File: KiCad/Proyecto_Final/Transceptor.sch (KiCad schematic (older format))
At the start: 51 parts, among them T1 2450BL05A0100, U1 MAX1193ETI+, U2 MAX2837

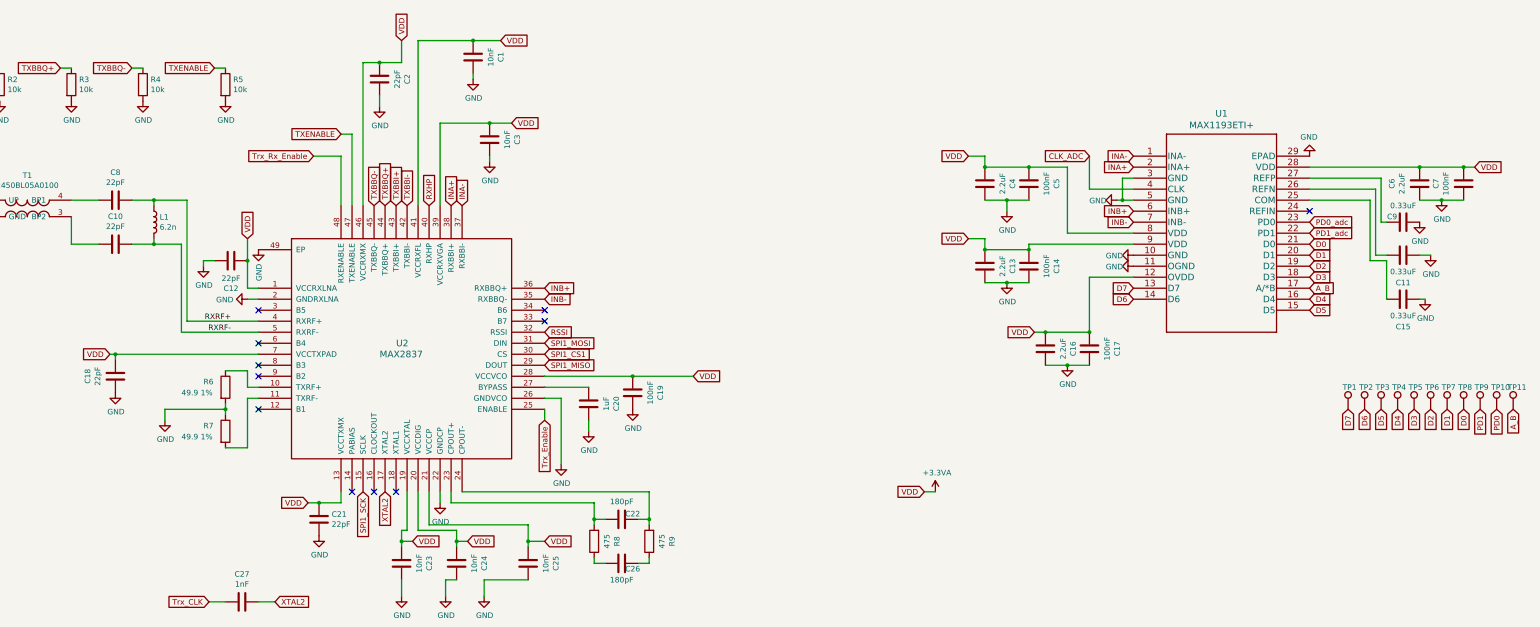
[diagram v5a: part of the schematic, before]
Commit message: Pistas reacomodadas para mejor ruteo.
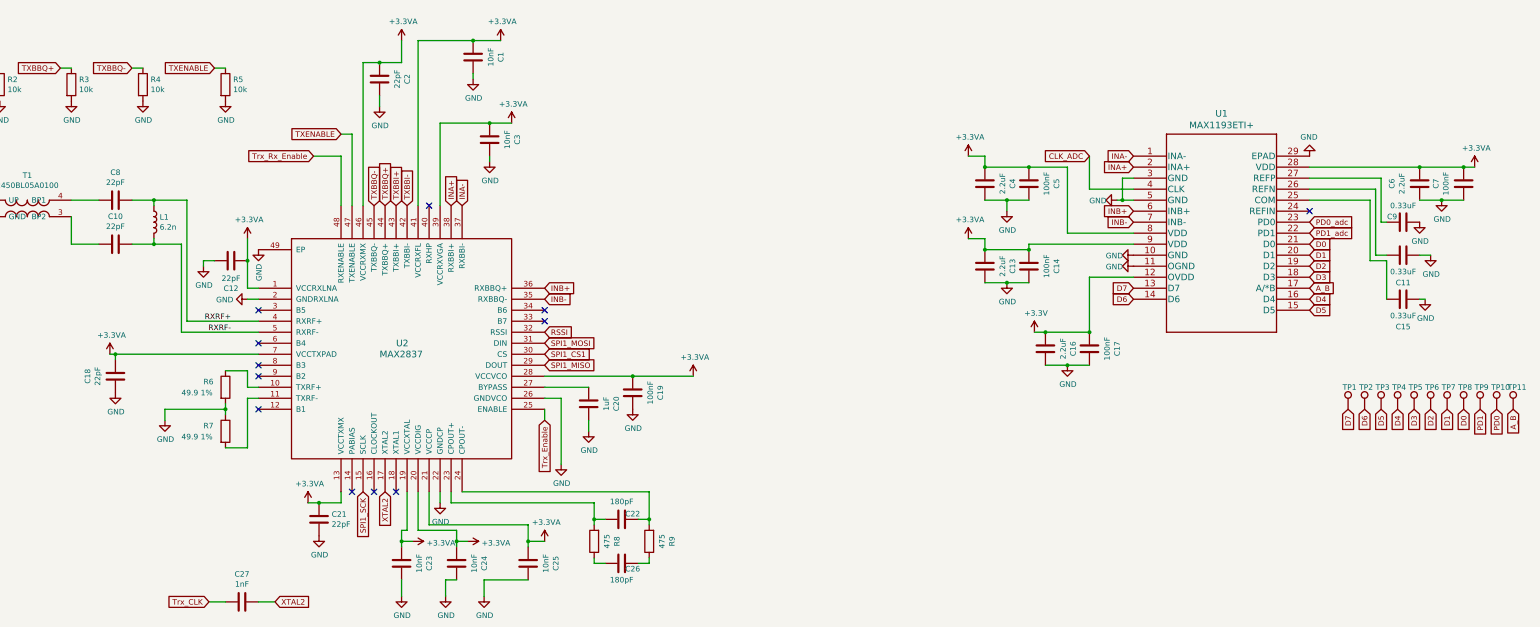
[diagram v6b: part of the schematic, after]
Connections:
- net +3.3VA: no longer C16.2, C17.2, U1.12 (OVDD)
- net RXHP: no longer names the net of U2.40 (RXHP)
- new net +3V3: C16.2, C17.2, U1.12 (OVDD)
- no-connect marks 11 -> 12
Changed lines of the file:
@@
 Wire Wire Line
 	5650 5950 5650 5800
-Text GLabel 5750 5450 2    50   Input ~ 0
-VDD
 Connection ~ 5650 5450
 Wire Wire Line
@@
 	1    0    0    -1
 $EndComp
-Text GLabel 6250 5450 2    50   Input ~ 0
-VDD
 Wire Wire Line
 	6050 5800 6050 5950
@@
 	-1   0    0    1
 $EndComp
-Text GLabel 6950 5450 2    50   Input ~ 0
-VDD
 Wire Wire Line
 	5900 5300 6800 5300
@@
 	1    0    0    -1
 $EndComp
-Text GLabel 8300 3950 2    50   Input ~ 0
-VDD
 Text GLabel 6950 3850 2    50   Input ~ 0
 SPI1_MISO
@@
 Wire Wire Line
 	6000 2400 6000 1650
-Text GLabel 6650 1650 2    50   Input ~ 0
-VDD
 Wire Wire Line
 	6650 1650 6450 1650
 Connection ~ 6450 1650
-Text GLabel 6550 900  2    50   Input ~ 0
-VDD
 $Comp
 L Device:C C1
@@
 Wire Wire Line
 	5450 1500 5450 1400
-Text GLabel 5650 900  1    50   Input ~ 0
-VDD
 Wire Wire Line
 	5650 900  5650 1100
@@
 Wire Wire Line
 	10800 1950 10950 1950
-Text GLabel 10800 1950 0    50   Input ~ 0
-VDD
 Wire Wire Line
 	11150 2350 10950 2350
@@
 Wire Wire Line
 	10950 2800 11350 2800
-Text GLabel 10800 2700 0    50   Input ~ 0
-VDD
 Wire Wire Line
 	10800 2700 10950 2700
@@
 	-1   0    0    1
 $EndComp
-Text GLabel 11400 3550 0    50   Input ~ 0
-VDD
 Wire Wire Line
 	11900 3050 12300 3050
-Text GLabel 15400 2050 2    50   Input ~ 0
-VDD
 Connection ~ 11900 3550
 $Comp
@@
 	1    0    0    -1
 $EndComp
-Text GLabel 3000 3750 0    50   Input ~ 0
-VDD
-Text GLabel 4250 2700 1    50   Input ~ 0
-VDD
 Wire Wire Line
 	4250 2700 4250 2900
@@
 Wire Wire Line
 	5100 5100 4900 5100
-Text GLabel 4800 5100 0    50   Input ~ 0
-VDD
 Wire Wire Line
 	4800 5100 4900 5100
@@
 Text GLabel 1300 1150 0    50   Input ~ 0
 TXBBI-
-Text GLabel 5900 2400 1    50   Input ~ 0
-RXHP
 Wire Wire Line
 	6000 1650 6450 1650
@@
 	11900 2250 12300 2250
 NoConn ~ 13900 2450
-Text GLabel 10400 5000 0    50   Input ~ 0
-VDD
-Wire Wire Line
-	10400 5000 10500 5000
 NoConn ~ 5600 5000
 $Comp
@@
 Wire Wire Line
 	4050 4250 4050 4300
-$Comp
-L power:+3.3VA #PWR?
-U 1 1 60A0F8F4
-P 10500 5000
-F 0 "#PWR?" H 10500 4850 50  0001 C CNN
-F 1 "+3.3VA" H 10515 5173 50  0000 C CNN
-F 2 "" H 10500 5000 50  0001 C CNN
-F 3 "" H 10500 5000 50  0001 C CNN
-	1    10500 5000
-	1    0    0    -1
-$EndComp
+NoConn ~ 5900 2400
+$Comp
+L power:+3.3VA #PWR0132
+U 1 1 609C56C0
+P 8300 3950
+F 0 "#PWR0132" H 8300 3800 50  0001 C CNN
+F 1 "+3.3VA" H 8315 4123 50  0000 C CNN
+F 2 "" H 8300 3950 50  0001 C CNN
+F 3 "" H 8300 3950 50  0001 C CNN
+	1    8300 3950
+	1    0    0    -1
+$EndComp
+$Comp
+L power:+3.3VA #PWR0133
+U 1 1 609C63F1
+P 6950 5450
+F 0 "#PWR0133" H 6950 5300 50  0001 C CNN
+F 1 "+3.3VA" H 6965 5623 50  0000 C CNN
+F 2 "" H 6950 5450 50  0001 C CNN
+F 3 "" H 6950 5450 50  0001 C CNN
+	1    6950 5450
+	1    0    0    -1
+$EndComp
+$Comp
+L power:+3.3VA #PWR0134
+U 1 1 609C66C1
+P 6250 5450
+F 0 "#PWR0134" H 6250 5300 50  0001 C CNN
+F 1 "+3.3VA" V 6265 5578 50  0000 L CNN
+F 2 "" H 6250 5450 50  0001 C CNN
+F 3 "" H 6250 5450 50  0001 C CNN
+	1    6250 5450
+	0    1    1    0
+$EndComp
+$Comp
+L power:+3.3VA #PWR0135
+U 1 1 609C6F0F
+P 5750 5450
+F 0 "#PWR0135" H 5750 5300 50  0001 C CNN
+F 1 "+3.3VA" V 5765 5578 50  0000 L CNN
+F 2 "" H 5750 5450 50  0001 C CNN
+F 3 "" H 5750 5450 50  0001 C CNN
+	1    5750 5450
+	0    1    1    0
+$EndComp
+$Comp
+L power:+3.3VA #PWR0136
+U 1 1 609C777F
+P 4800 5100
+F 0 "#PWR0136" H 4800 4950 50  0001 C CNN
+F 1 "+3.3VA" H 4815 5273 50  0000 C CNN
+F 2 "" H 4800 5100 50  0001 C CNN
+F 3 "" H 4800 5100 50  0001 C CNN
+	1    4800 5100
+	1    0    0    -1
+$EndComp
+$Comp
+L power:+3.3VA #PWR0137
+U 1 1 609C8000
+P 3000 3750
+F 0 "#PWR0137" H 3000 3600 50  0001 C CNN
+F 1 "+3.3VA" H 3015 3923 50  0000 C CNN
+F 2 "" H 3000 3750 50  0001 C CNN
+F 3 "" H 3000 3750 50  0001 C CNN
+	1    3000 3750
+	1    0    0    -1
+$EndComp
+$Comp
+L power:+3.3VA #PWR0138
+U 1 1 609C88CB
+P 4250 2700
+F 0 "#PWR0138" H 4250 2550 50  0001 C CNN
+F 1 "+3.3VA" H 4265 2873 50  0000 C CNN
+F 2 "" H 4250 2700 50  0001 C CNN
+F 3 "" H 4250 2700 50  0001 C CNN
+	1    4250 2700
+	1    0    0    -1
+$EndComp
+$Comp
+L power:+3.3VA #PWR0139
+U 1 1 609C914C
+P 5650 900
+F 0 "#PWR0139" H 5650 750 50  0001 C CNN
+F 1 "+3.3VA" H 5665 1073 50  0000 C CNN
+F 2 "" H 5650 900 50  0001 C CNN
+F 3 "" H 5650 900 50  0001 C CNN
+	1    5650 900
+	1    0    0    -1
+$EndComp
+$Comp
+L power:+3.3VA #PWR0140
+U 1 1 609C9988
+P 6550 900
+F 0 "#PWR0140" H 6550 750 50  0001 C CNN
+F 1 "+3.3VA" H 6565 1073 50  0000 C CNN
+F 2 "" H 6550 900 50  0001 C CNN
+F 3 "" H 6550 900 50  0001 C CNN
+	1    6550 900
+	1    0    0    -1
+$EndComp
+$Comp
+L power:+3.3VA #PWR0141
+U 1 1 609CA2CB
+P 6650 1650
+F 0 "#PWR0141" H 6650 1500 50  0001 C CNN
+F 1 "+3.3VA" H 6665 1823 50  0000 C CNN
+F 2 "" H 6650 1650 50  0001 C CNN
+F 3 "" H 6650 1650 50  0001 C CNN
+	1    6650 1650
+	1    0    0    -1
+$EndComp
+$Comp
+L power:+3.3VA #PWR0142
+U 1 1 609CB87B
+P 10800 1950
+F 0 "#PWR0142" H 10800 1800 50  0001 C CNN
+F 1 "+3.3VA" H 10815 2123 50  0000 C CNN
+F 2 "" H 10800 1950 50  0001 C CNN
+F 3 "" H 10800 1950 50  0001 C CNN
+	1    10800 1950
+	1    0    0    -1
+$EndComp
+$Comp
+L power:+3.3VA #PWR0143
+U 1 1 609CC15F
+P 10800 2700
+F 0 "#PWR0143" H 10800 2550 50  0001 C CNN
+F 1 "+3.3VA" H 10815 2873 50  0000 C CNN
+F 2 "" H 10800 2700 50  0001 C CNN
+F 3 "" H 10800 2700 50  0001 C CNN
+	1    10800 2700
+	1    0    0    -1
+$EndComp
+$Comp
+L power:+3.3VA #PWR0144
+U 1 1 609CCA9E
+P 15400 2050
+F 0 "#PWR0144" H 15400 1900 50  0001 C CNN
+F 1 "+3.3VA" H 15415 2223 50  0000 C CNN
+F 2 "" H 15400 2050 50  0001 C CNN
+F 3 "" H 15400 2050 50  0001 C CNN
+	1    15400 2050
+	1    0    0    -1
+$EndComp
+$Comp
+L power:+3.3V #PWR0145
+U 1 1 609CD9E1
+P 11400 3550
+F 0 "#PWR0145" H 11400 3400 50  0001 C CNN
+F 1 "+3.3V" H 11415 3723 50  0000 C CNN
+F 2 "" H 11400 3550 50  0001 C CNN
+F 3 "" H 11400 3550 50  0001 C CNN
+	1    11400 3550
+	1    0    0    -1
+$EndComp

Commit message: Avances PCB.
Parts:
- removed TP1, TP2, TP3, TP4, TP5, TP6, TP7, TP8: TestPoint, TestPoint:TestPoint_Pad_D1.0mm, symbol Connector:TestPoint
- TP1: renamed from TP9; footprint TestPoint:TestPoint_Pad_D1.0mm -> Tesis2020-21:TestPoint_Mask_D0.4mm
- TP2: renamed from TP10; footprint TestPoint:TestPoint_Pad_D1.0mm -> Tesis2020-21:TestPoint_Mask_D0.4mm
- TP3: renamed from TP11; footprint TestPoint:TestPoint_Pad_D1.0mm -> Tesis2020-21:TestPoint_Mask_D0.4mm
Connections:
- net PD0 is gone; now on net PD0_adc: TP2.1
- net PD1 is gone; now on net PD1_adc: TP1.1

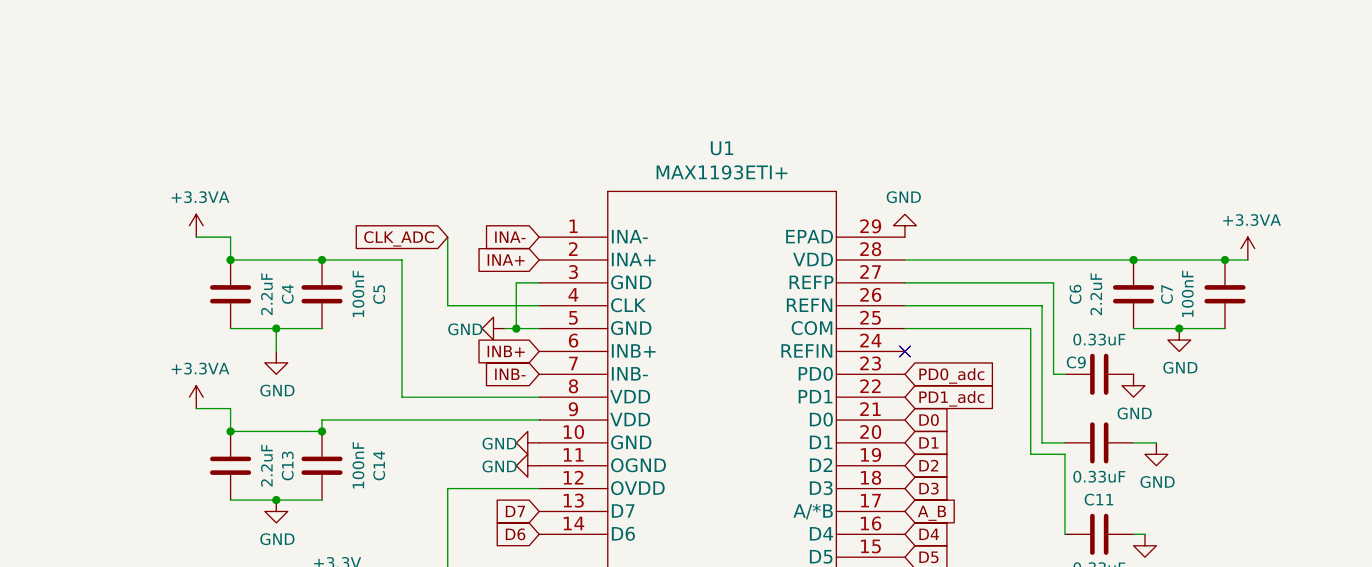
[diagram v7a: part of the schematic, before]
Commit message: Falta logo utn.
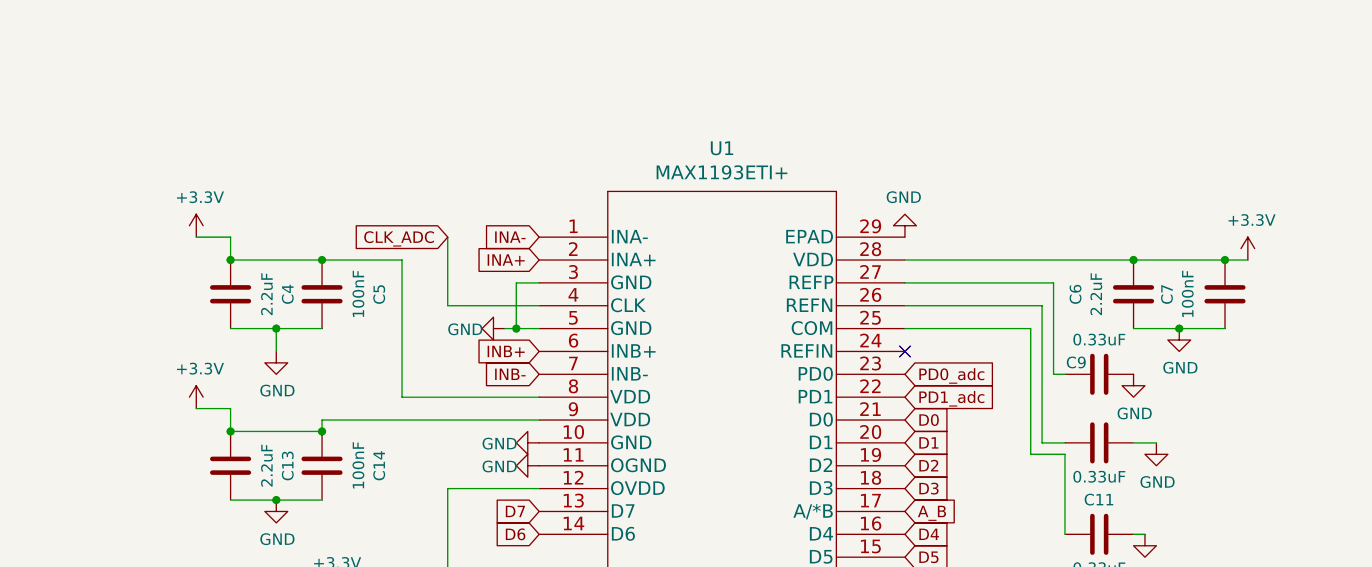
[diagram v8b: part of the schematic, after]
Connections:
- net +3.3VA: no longer C13.2, C14.2, C4.2, C5.2, C6.1, C7.1, U1.28 (VDD), U1.8 (VDD), U1.9 (VDD)
- net +3V3: now also C13.2, C14.2, C4.2, C5.2, C6.1, C7.1, U1.28 (VDD), U1.8 (VDD), U1.9 (VDD)
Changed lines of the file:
@@
-$EndComp
-$Comp
-L power:+3.3VA #PWR011
-U 1 1 609CB87B
-P 10800 1950
-F 0 "#PWR011" H 10800 1800 50  0001 C CNN
-F 1 "+3.3VA" H 10815 2123 50  0000 C CNN
-F 2 "" H 10800 1950 50  0001 C CNN
-F 3 "" H 10800 1950 50  0001 C CNN
-	1    10800 1950
-	1    0    0    -1
-$EndComp
-$Comp
-L power:+3.3VA #PWR020
-U 1 1 609CC15F
-P 10800 2700
-F 0 "#PWR020" H 10800 2550 50  0001 C CNN
-F 1 "+3.3VA" H 10815 2873 50  0000 C CNN
-F 2 "" H 10800 2700 50  0001 C CNN
-F 3 "" H 10800 2700 50  0001 C CNN
-	1    10800 2700
-	1    0    0    -1
-$EndComp
-$Comp
-L power:+3.3VA #PWR014
-U 1 1 609CCA9E
-P 15400 2050
-F 0 "#PWR014" H 15400 1900 50  0001 C CNN
-F 1 "+3.3VA" H 15415 2223 50  0000 C CNN
-F 2 "" H 15400 2050 50  0001 C CNN
-F 3 "" H 15400 2050 50  0001 C CNN
-	1    15400 2050
-	1    0    0    -1
 $EndComp
 $Comp
@@
 	1    0    0    -1
 $EndComp
+$Comp
+L power:+3.3V #PWR0146
+U 1 1 60A6D92C
+P 10800 1950
+F 0 "#PWR0146" H 10800 1800 50  0001 C CNN
+F 1 "+3.3V" H 10815 2123 50  0000 C CNN
+F 2 "" H 10800 1950 50  0001 C CNN
+F 3 "" H 10800 1950 50  0001 C CNN
+	1    10800 1950
+	1    0    0    -1
+$EndComp
+$Comp
+L power:+3.3V #PWR0147
+U 1 1 60A6E016
+P 10800 2700
+F 0 "#PWR0147" H 10800 2550 50  0001 C CNN
+F 1 "+3.3V" H 10815 2873 50  0000 C CNN
+F 2 "" H 10800 2700 50  0001 C CNN
+F 3 "" H 10800 2700 50  0001 C CNN
+	1    10800 2700
+	1    0    0    -1
+$EndComp
+$Comp
+L power:+3.3V #PWR0148
+U 1 1 60A6E58E
+P 15400 2050
+F 0 "#PWR0148" H 15400 1900 50  0001 C CNN
+F 1 "+3.3V" H 15415 2223 50  0000 C CNN
+F 2 "" H 15400 2050 50  0001 C CNN
+F 3 "" H 15400 2050 50  0001 C CNN
+	1    15400 2050
+	1    0    0    -1
+$EndComp
